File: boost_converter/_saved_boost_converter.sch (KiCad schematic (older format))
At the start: 34 parts, among them J1 Battery +, J2 GND, Q1 N Channel, Q2 N Channel, Q3 N Channel, U1 LM5122

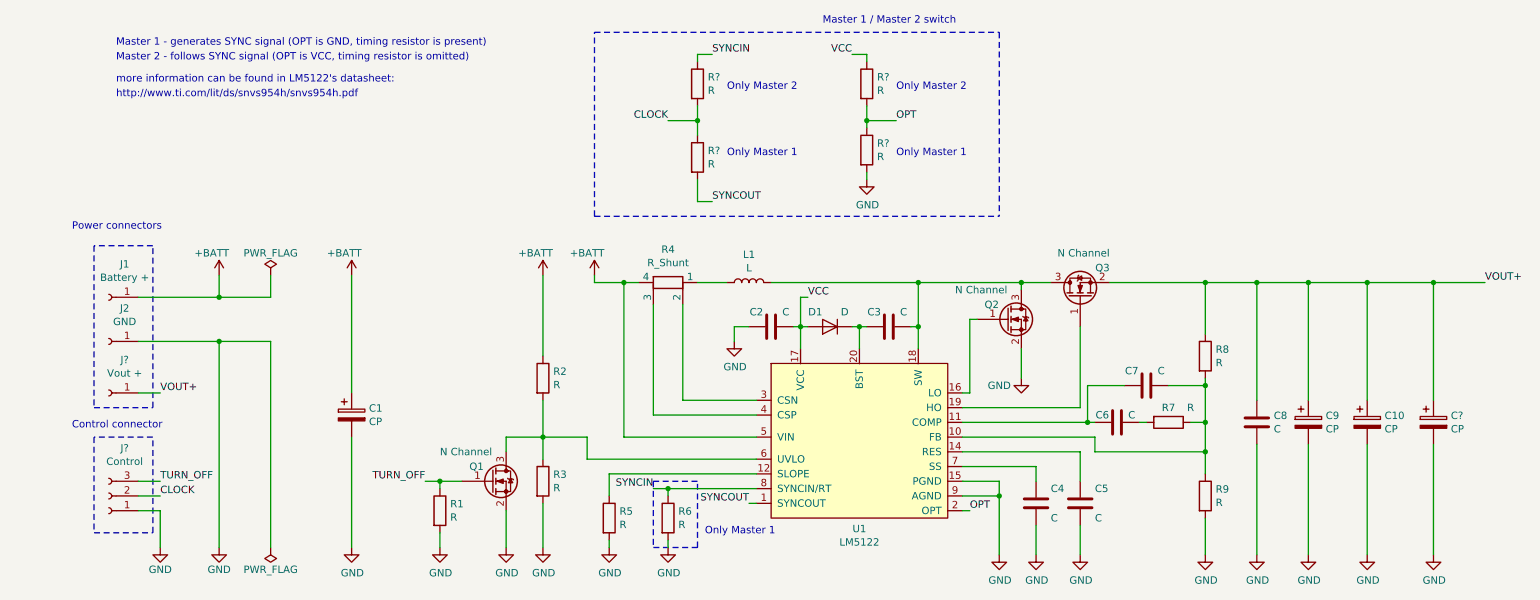
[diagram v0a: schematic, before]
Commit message: Added Multi phase synchronisation
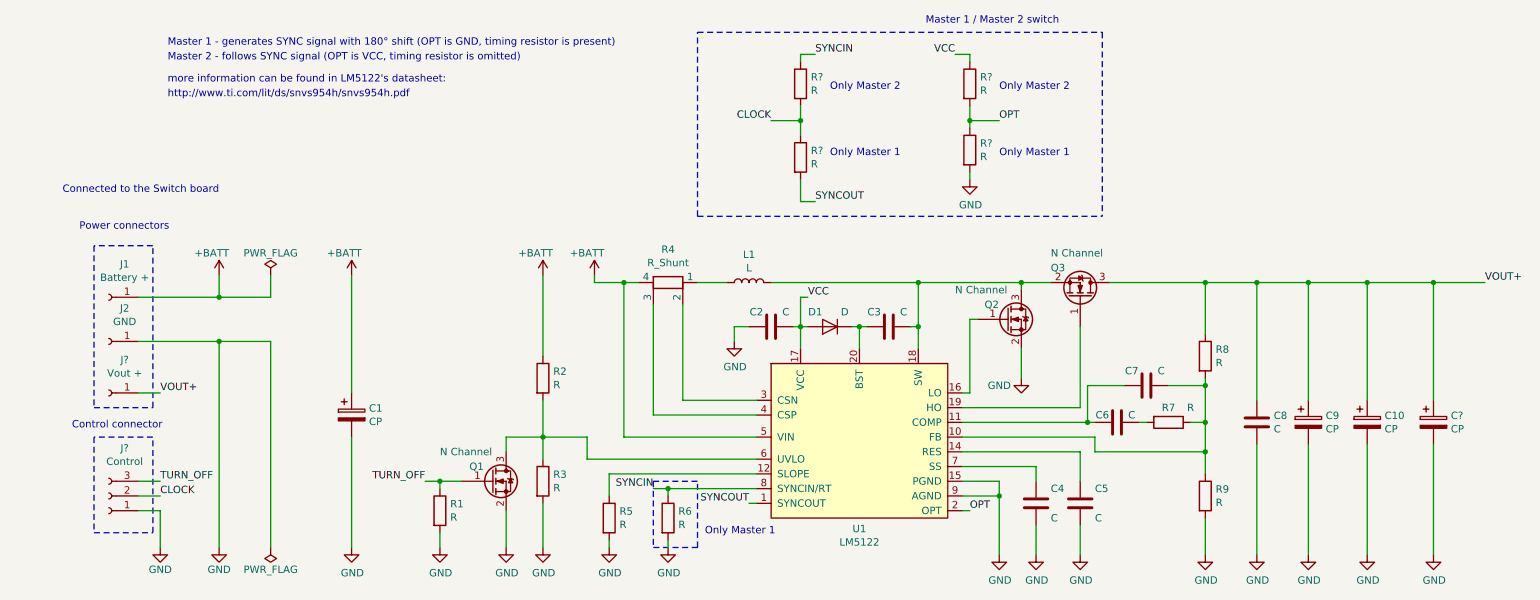
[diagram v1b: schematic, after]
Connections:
- net VOUT+: now also Q3.3 (D); no longer Q3.2 (S)
- net at C3.1, L1.2, Q2.3 (D)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: now also Q3.2 (S); no longer Q3.3 (D)
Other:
- note added: "Connected to the Switch board"
- note added: "Master 1 - generates SYNC signal with 180° shift (OPT is GND, timing resistor is present)"
- note removed: "Master 1 - generates SYNC signal (OPT is GND, timing resistor is present)"
- moved on the sheet: R?
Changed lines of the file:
@@
 F 3 "https://www.infineon.com/dgdl/Infineon-BSS214NW-DS-v02_02-en.pdf?fileId=db3a30431b3e89eb011b695aebc01bde" H 7750 3550 50  0001 L CNN
 	1    7750 3550
-	0    -1   -1   0
+	0    1    -1   0
 $EndComp
 Wire Wire Line
@@
 Wire Notes Line
 	1050 3200 1050 4300
-Text Notes 900  3100 0    50   ~ 0
+Text Notes 950  3100 0    50   ~ 0
 Power connectors\n
 Wire Wire Line
@@
 Wire Wire Line
 	6950 5000 7000 5000
-Text Label 6500 2350 0    50   ~ 0
+Text Label 7200 2350 0    50   ~ 0
 OPT
 $Comp
 L power:GND #PWR?
 U 1 1 5CA907A4
-P 6300 2750
-F 0 "#PWR?" H 6300 2500 50  0001 C CNN
-F 1 "GND" H 6305 2577 50  0000 C CNN
-F 2 "" H 6300 2750 50  0001 C CNN
-F 3 "" H 6300 2750 50  0001 C CNN
-	1    6300 2750
+P 7000 2750
+F 0 "#PWR?" H 7000 2500 50  0001 C CNN
+F 1 "GND" H 7005 2577 50  0000 C CNN
+F 2 "" H 7000 2750 50  0001 C CNN
+F 3 "" H 7000 2750 50  0001 C CNN
+	1    7000 2750
 	1    0    0    -1
 $EndComp
@@
 Wire Wire Line
 	5850 3550 5900 3550
-Text Label 6200 1900 2    50   ~ 0
+Text Label 6900 1900 2    50   ~ 0
 VCC
 $Comp
 L Device:R R?
 U 1 1 5CA94C86
-P 6300 2100
-F 0 "R?" H 6370 2146 50  0000 L CNN
-F 1 "R" H 6370 2055 50  0000 L CNN
-F 2 "" V 6230 2100 50  0001 C CNN
-F 3 "~" H 6300 2100 50  0001 C CNN
-	1    6300 2100
+P 7000 2100
+F 0 "R?" H 7070 2146 50  0000 L CNN
+F 1 "R" H 7070 2055 50  0000 L CNN
+F 2 "" V 6930 2100 50  0001 C CNN
+F 3 "~" H 7000 2100 50  0001 C CNN
+	1    7000 2100
 	1    0    0    -1
 $EndComp
@@
 L Device:R R?
 U 1 1 5CA987EA
-P 6300 2550
-F 0 "R?" H 6370 2596 50  0000 L CNN
-F 1 "R" H 6370 2505 50  0000 L CNN
-F 2 "" V 6230 2550 50  0001 C CNN
-F 3 "~" H 6300 2550 50  0001 C CNN
-	1    6300 2550
-	1    0    0    -1
-$EndComp
-Wire Wire Line
-	6300 2750 6300 2700
-Wire Wire Line
-	6300 2400 6300 2350
-Wire Wire Line
-	6500 2350 6300 2350
-Connection ~ 6300 2350
-Wire Wire Line
-	6300 2350 6300 2250
-Wire Wire Line
-	6200 1900 6300 1900
-Wire Wire Line
-	6300 1900 6300 1950
-Wire Notes Line
-	7200 1750 7200 3000
-Wire Notes Line
-	4450 3000 4450 1750
-Text Notes 6000 1700 0    50   ~ 0
+P 7000 2550
+F 0 "R?" H 7070 2596 50  0000 L CNN
+F 1 "R" H 7070 2505 50  0000 L CNN
+F 2 "" V 6930 2550 50  0001 C CNN
+F 3 "~" H 7000 2550 50  0001 C CNN
+	1    7000 2550
+	1    0    0    -1
+$EndComp
+Wire Wire Line
+	7000 2750 7000 2700
+Wire Wire Line
+	7000 2400 7000 2350
+Wire Wire Line
+	7200 2350 7000 2350
+Connection ~ 7000 2350
+Wire Wire Line
+	7000 2350 7000 2250
+Wire Wire Line
+	6900 1900 7000 1900
+Wire Wire Line
+	7000 1900 7000 1950
+Wire Notes Line
+	7900 1750 7900 3000
+Wire Notes Line
+	5150 3000 5150 1750
+Text Notes 6700 1700 0    50   ~ 0
 Master 1 / Master 2 switch\n
 Wire Wire Line
@@
 	4850 4850 4950 4850
 Connection ~ 4950 4850
-Text Label 4950 2350 2    50   ~ 0
+Text Label 5650 2350 2    50   ~ 0
 CLOCK
 Wire Wire Line
@@
 Wire Wire Line
 	5500 4950 5550 4950
-Text Label 5250 1900 0    50   ~ 0
+Text Label 5950 1900 0    50   ~ 0
 SYNCIN
-Text Label 5250 2900 0    50   ~ 0
+Text Label 5950 2900 0    50   ~ 0
 SYNCOUT
 $Comp
 L Device:R R?
 U 1 1 5CAD84E3
-P 5150 2100
-F 0 "R?" H 5220 2146 50  0000 L CNN
-F 1 "R" H 5220 2055 50  0000 L CNN
-F 2 "" V 5080 2100 50  0001 C CNN
-F 3 "~" H 5150 2100 50  0001 C CNN
-	1    5150 2100
+P 5850 2100
+F 0 "R?" H 5920 2146 50  0000 L CNN
+F 1 "R" H 5920 2055 50  0000 L CNN
+F 2 "" V 5780 2100 50  0001 C CNN
+F 3 "~" H 5850 2100 50  0001 C CNN
+	1    5850 2100
 	1    0    0    -1
 $EndComp
@@
 L Device:R R?
 U 1 1 5CAD8BE8
-P 5150 2600
-F 0 "R?" H 5220 2646 50  0000 L CNN
-F 1 "R" H 5220 2555 50  0000 L CNN
-F 2 "" V 5080 2600 50  0001 C CNN
-F 3 "~" H 5150 2600 50  0001 C CNN
-	1    5150 2600
-	1    0    0    -1
-$EndComp
-Wire Wire Line
-	4950 2350 5150 2350
-Wire Wire Line
-	5150 2350 5150 2250
-Wire Wire Line
-	5150 2450 5150 2350
-Connection ~ 5150 2350
-Wire Wire Line
-	5250 1900 5150 1900
-Wire Wire Line
-	5150 1900 5150 1950
-Wire Wire Line
-	5250 2900 5150 2900
-Wire Wire Line
-	5150 2900 5150 2750
+P 5850 2600
+F 0 "R?" H 5920 2646 50  0000 L CNN
+F 1 "R" H 5920 2555 50  0000 L CNN
+F 2 "" V 5780 2600 50  0001 C CNN
+F 3 "~" H 5850 2600 50  0001 C CNN
+	1    5850 2600
+	1    0    0    -1
+$EndComp
+Wire Wire Line
+	5650 2350 5850 2350
+Wire Wire Line
+	5850 2350 5850 2250
+Wire Wire Line
+	5850 2450 5850 2350
+Connection ~ 5850 2350
+Wire Wire Line
+	5950 1900 5850 1900
+Wire Wire Line
+	5850 1900 5850 1950
+Wire Wire Line
+	5950 2900 5850 2900
+Wire Wire Line
+	5850 2900 5850 2750
 Wire Wire Line
 	4400 4650 4400 4500
@@
 Wire Notes Line
 	5150 4800 4850 4800
-Text Notes 5350 2600 0    50   ~ 0
+Text Notes 6050 2600 0    50   ~ 0
 Only Master 1\n
-Text Notes 6500 2600 0    50   ~ 0
+Text Notes 7200 2600 0    50   ~ 0
 Only Master 1\n
 Wire Notes Line
-	4450 3000 7200 3000
-Wire Notes Line
-	4450 1750 7200 1750
-Text Notes 6500 2150 0    50   ~ 0
+	5150 3000 7900 3000
+Wire Notes Line
+	5150 1750 7900 1750
+Text Notes 7200 2150 0    50   ~ 0
 Only Master 2\n
-Text Notes 5350 2150 0    50   ~ 0
+Text Notes 6050 2150 0    50   ~ 0
 Only Master 2\n
-Text Notes 1200 1850 0    50   ~ 0
-Master 1 - generates SYNC signal (OPT is GND, timing resistor is present)
-Text Notes 1200 1950 0    50   ~ 0
+Text Notes 1550 1850 0    50   ~ 0
+Master 1 - generates SYNC signal with 180° shift (OPT is GND, timing resistor is present)
+Text Notes 1550 1950 0    50   ~ 0
 Master 2 - follows SYNC signal (OPT is VCC, timing resistor is omitted)
-Text Notes 1200 2100 0    50   ~ 0
+Text Notes 1550 2100 0    50   ~ 0
 more information can be found in LM5122's datasheet:
-Text Notes 1200 2200 0    50   ~ 0
+Text Notes 1550 2200 0    50   ~ 0
 http://www.ti.com/lit/ds/snvs954h/snvs954h.pdf\n
 Wire Wire Line
@@
 Wire Wire Line
 	10150 3450 10500 3450
+Text Notes 1900 2850 2    50   ~ 0
+Connected to the Switch board
 $EndSCHEMATC
